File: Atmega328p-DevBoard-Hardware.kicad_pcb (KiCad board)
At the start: 2 copper layers, 55 parts, among them J1 PWR_IN, J2 DBG/PROG, J3 MTR1-CON, J4 MTR2-CON, SW1 SW_SPST, SW2 SW_SPST, U1 L7805, U2 ATmega328P-A, U3 L293D, U4 CD4511BE, U5 SC39-11YWA, Y1 LFXTAL003237-Crystal-16MHz

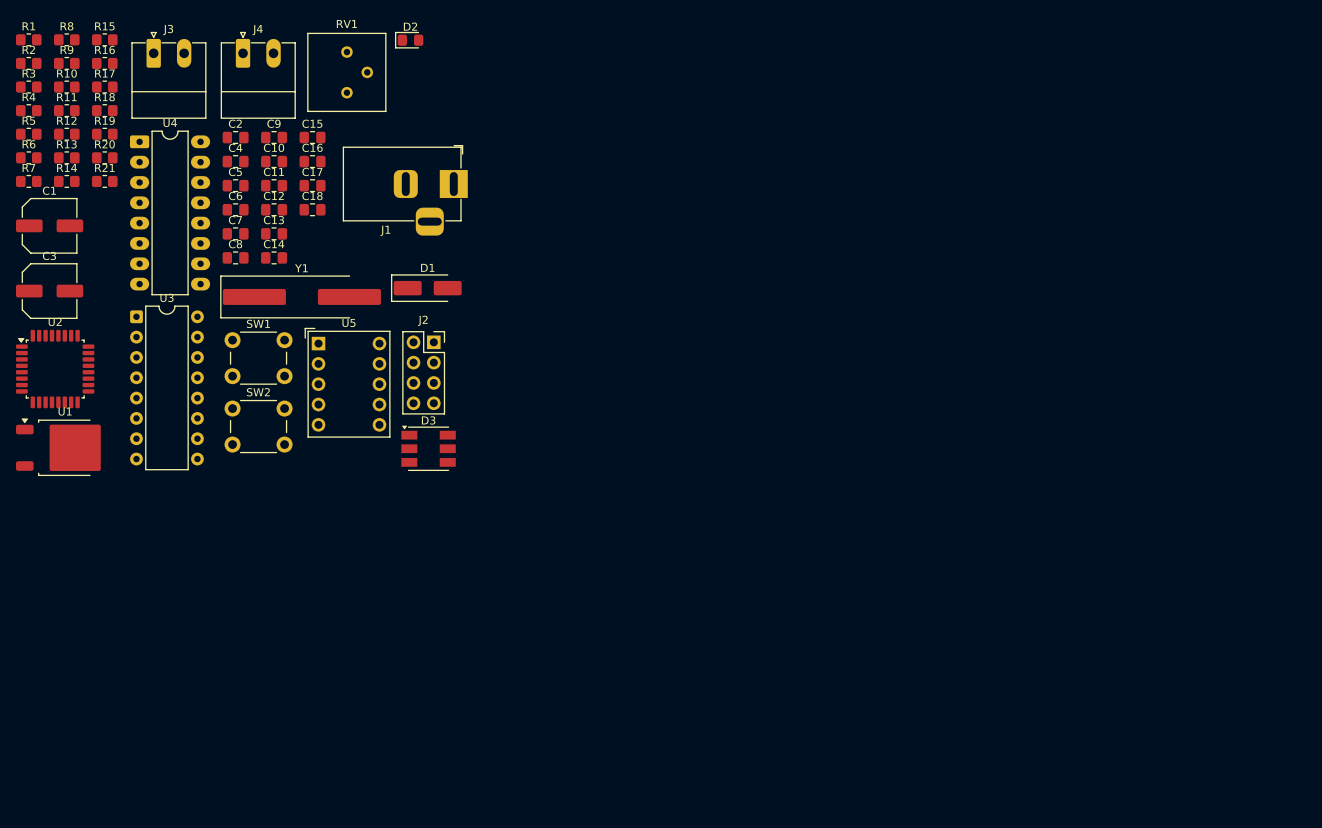
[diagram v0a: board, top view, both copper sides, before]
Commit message: Updated schematics wrt footprint selections and mounting holes, and pcb component placement in-progress
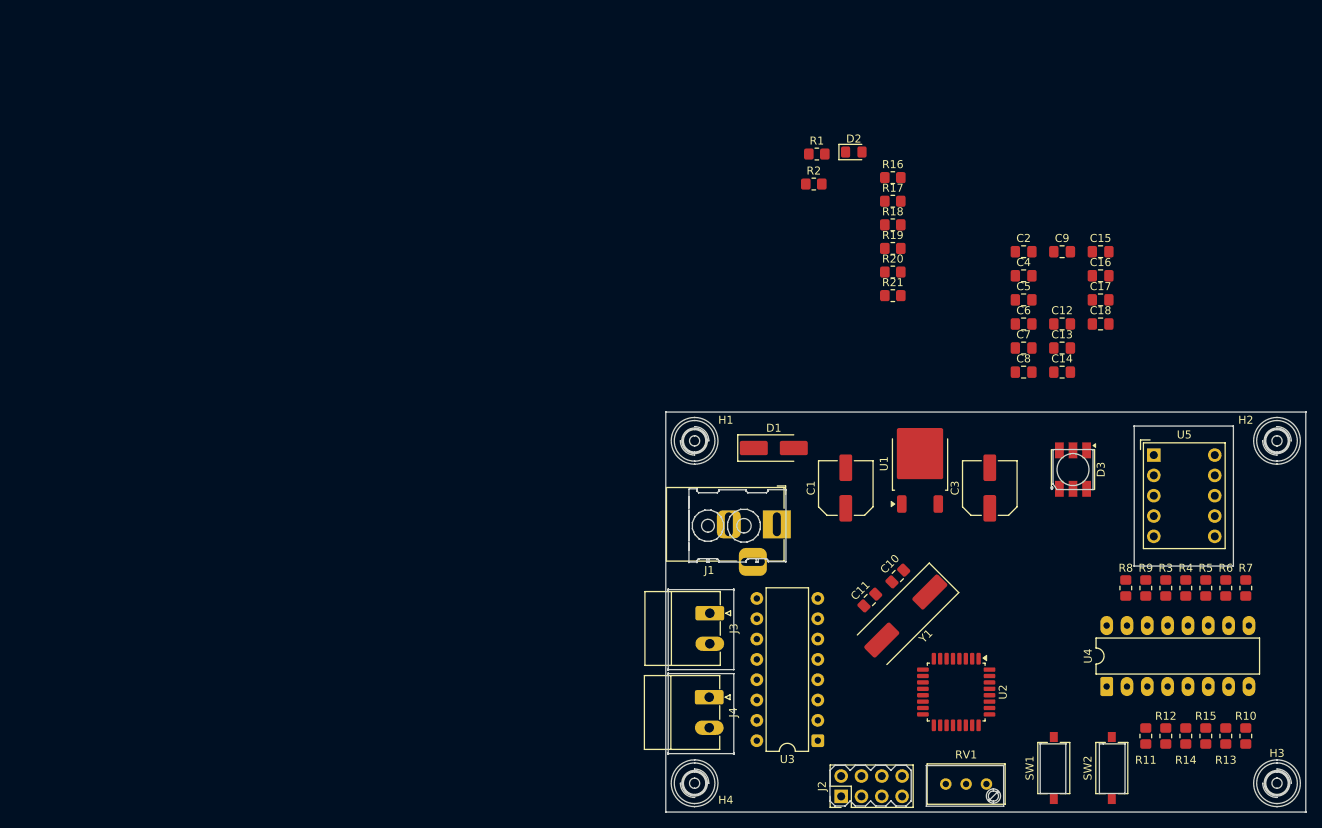
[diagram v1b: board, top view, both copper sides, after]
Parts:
- added H1: MountingHole, MountingHole:MountingHole_3.2mm_M3_DIN965, F.Cu at (113.6, 78.6)
- added H2: MountingHole, MountingHole:MountingHole_3.2mm_M3_DIN965, F.Cu at (186.4, 78.6)
- added H3: MountingHole, MountingHole:MountingHole_3.2mm_M3_DIN965, F.Cu at (186.4, 121.4)
- added H4: MountingHole, MountingHole:MountingHole_3.2mm_M3_DIN965, F.Cu at (113.6, 121.4)
- J2: footprint Connector_PinSocket_2.54mm:PinSocket_2x04_P2.54mm_Vertical -> Connector_PinHeader_2.54mm:PinHeader_2x04_P2.54mm_Vertical
- RV1: footprint Potentiometer_THT:Potentiometer_Bourns_3386P_Vertical -> Potentiometer_THT:Potentiometer_Bourns_3296W_Vertical
- SW1, SW2: footprint Button_Switch_THT:SW_PUSH_6mm -> Button_Switch_SMD:SW_Tactile_SPST_NO_Straight_CK_PTS636Sx25SMTRLFS
- Y1: footprint Crystal:Crystal_SMD_HC49-SD_HandSoldering -> Crystal:Crystal_SMD_HC49-SD
- moved R10 168.2 mm to (182.5, 115.5), turned to 90 degrees
- moved R15 162.8 mm to (177.5, 115.5), turned to 90 degrees
- moved R13 161.9 mm to (180.0, 115.5), turned to 90 degrees
- moved R7 160.4 mm to (182.5, 97.0), turned to 90 degrees
- moved R6 159.0 mm to (180.0, 97.0), turned to 90 degrees
- moved R5 157.7 mm to (177.5, 97.0), turned to 90 degrees
- moved R12 156.6 mm to (172.5, 115.5), turned to 90 degrees
- moved R4 156.5 mm to (175.0, 97.0), turned to 90 degrees
- moved R14 156.1 mm to (175.0, 115.5), turned to 90 degrees
- moved R11 155.9 mm to (170.0, 115.5), turned to 90 degrees
- moved R3 155.3 mm to (172.5, 97.0), turned to 90 degrees
- moved R9 150.0 mm to (170.0, 97.0), turned to 90 degrees
- moved R8 149.1 mm to (167.5, 97.0), turned to 90 degrees
- moved U4 138.7 mm to (165.1, 109.3), turned to 90 degrees
- moved C3 120.1 mm to (150.5, 84.5), turned to 90 degrees
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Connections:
- RV1 pad 1: +5V -> GND
- RV1 pad 3: GND -> +5V
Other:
- board outline added: 80.1 x 50.1 mm

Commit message: Updated Schematics and Footprints, Finished with Component Placements
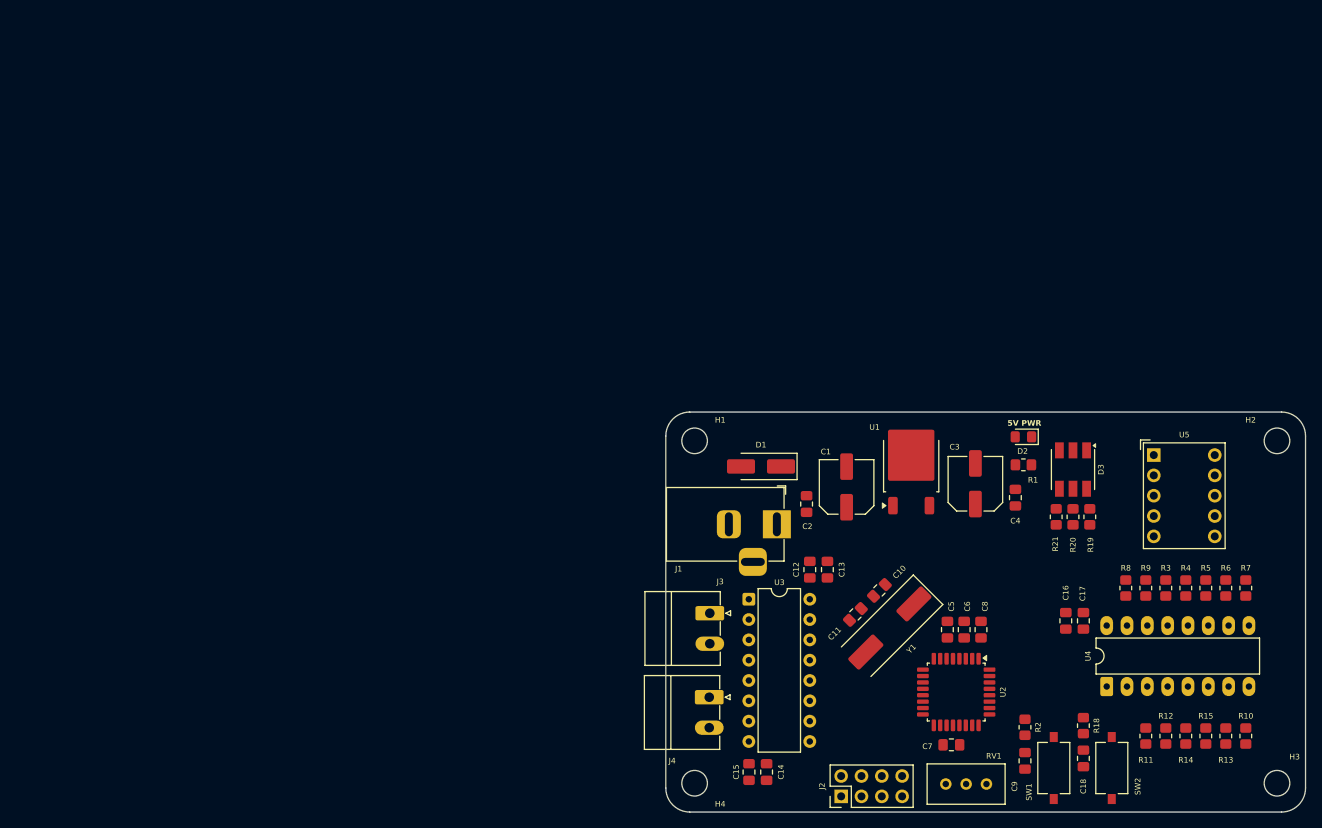
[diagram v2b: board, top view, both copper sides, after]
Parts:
- removed R16, R17: 0R, Resistor_SMD:R_0805_2012Metric_Pad1.20x1.40mm_HandSolder
- moved C15 78.5 mm to (120.4, 120.0), turned to -90 degrees
- moved R2 72.9 mm to (154.9, 114.4), turned to -90 degrees
- moved R18 67.0 mm to (162.2, 114.2), turned to -90 degrees
- moved C9 63.8 mm to (154.9, 118.6), turned to -90 degrees
- moved C14 62.2 mm to (122.6, 120.0), turned to -90 degrees
- moved C18 54.4 mm to (162.2, 118.3), turned to -90 degrees
- moved C7 50.4 mm to (145.7, 116.6)
- moved R1 46.6 mm to (154.7, 81.6), turned to 180 degrees
- moved C12 44.0 mm to (128.0, 94.7), turned to 90 degrees
- moved C16 43.3 mm to (160.0, 101.1), turned to 90 degrees
- moved C5 42.3 mm to (145.2, 102.2), turned to 90 degrees
- moved R19 41.6 mm to (163.0, 88.1), turned to 90 degrees
- moved C2 41.6 mm to (127.6, 86.5), turned to -90 degrees
- moved D2 41.4 mm to (154.7, 78.1), turned to 180 degrees
- moved C13 40.3 mm to (130.2, 94.7), turned to 90 degrees
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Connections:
- U2 pad 19: unconnected-(U2-ADC6-Pad19) -> /BLANKING_INPUT_BL
- U2 pad 22: unconnected-(U2-ADC7-Pad22) -> /LAMP_TEST_LT
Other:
- board size 80.1 x 50.1 mm -> 80 x 50 mm
- board text added: "5V PWR"
